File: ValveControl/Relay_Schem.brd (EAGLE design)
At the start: 101.6 x 53.6 mm, 69 parts, among them M1 IRLZ44, M2 IRLZ44, M3 IRLZ44, M4 IRLZ44, Q1 LINEAR_REGULATOR, Q2 LINEAR_REGULATOR, Q3 LINEAR_REGULATOR, Q4 LINEAR_REGULATOR, Q5 LINEAR_REGULATOR

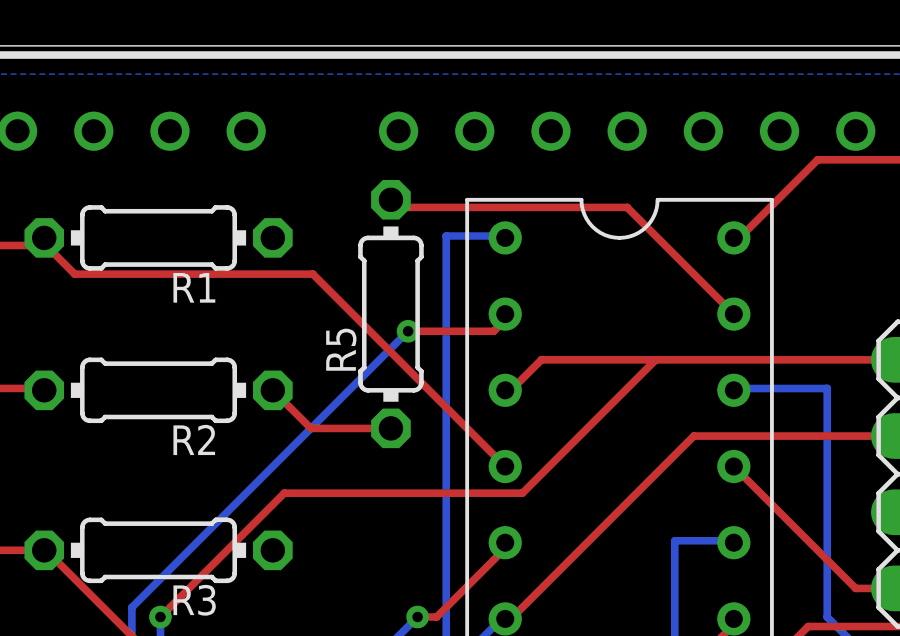
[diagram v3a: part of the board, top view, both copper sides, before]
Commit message: Some minor tweaks to the layout
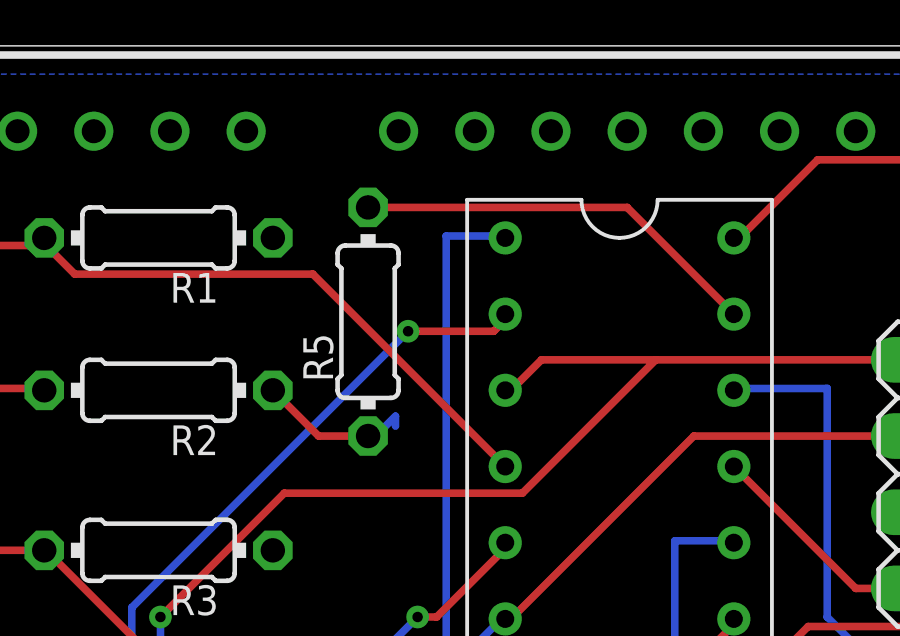
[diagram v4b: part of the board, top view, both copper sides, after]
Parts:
- moved R5 0.80 mm to (67.6, 44.5)
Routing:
- net N$10: track 13.0 -> 13.7 mm
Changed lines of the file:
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@@
 <attribute name="VALUE" x="60.1726" y="29.8704" size="0.9906" layer="27" ratio="10" rot="R180"/>
 </element>
-<element name="R5" library="rcl" library_urn="urn:adsk.eagle:library:334" package="0204/7" package3d_urn="urn:adsk.eagle:package:23498/2" value="10K" x="68.326" y="44.704" smashed="yes" rot="R90">
-<attribute name="NAME" x="67.1576" y="42.6974" size="0.9906" layer="25" ratio="10" rot="R90"/>
-<attribute name="POPULARITY" value="48" x="68.326" y="44.704" size="1.778" layer="27" rot="R90" display="off"/>
-<attribute name="SPICEPREFIX" value="R" x="68.326" y="44.704" size="1.778" layer="27" rot="R90" display="off"/>
-<attribute name="VALUE" x="66.8274" y="45.1104" size="0.9906" layer="27" ratio="10" rot="R90"/>
+<element name="R5" library="rcl" library_urn="urn:adsk.eagle:library:334" package="0204/7" package3d_urn="urn:adsk.eagle:package:23498/2" value="10K" x="67.564" y="44.45" smashed="yes" rot="R90">
+<attribute name="NAME" x="66.3956" y="42.4434" size="0.9906" layer="25" ratio="10" rot="R90"/>
+<attribute name="POPULARITY" value="48" x="67.564" y="44.45" size="1.778" layer="27" rot="R90" display="off"/>
+<attribute name="SPICEPREFIX" value="R" x="67.564" y="44.45" size="1.778" layer="27" rot="R90" display="off"/>
+<attribute name="VALUE" x="66.0654" y="44.8564" size="0.9906" layer="27" ratio="10" rot="R90"/>
 </element>
 <element name="R6" library="rcl" library_urn="urn:adsk.eagle:library:334" package="0204/7" package3d_urn="urn:adsk.eagle:package:23498/2" value="10K" x="63.246" y="21.59" smashed="yes" rot="R180">
@@
 <contactref element="M3" pad="3"/>
 <contactref element="M4" pad="3"/>
-<wire x1="68.4784" y1="41.3004" x2="68.326" y2="41.148" width="0.254" layer="16"/>
-<wire x1="68.326" y1="41.148" x2="68.326" y2="40.894" width="0.254" layer="16"/>
+<wire x1="68.4784" y1="41.3004" x2="67.818" y2="40.64" width="0.254" layer="16"/>
+<wire x1="67.818" y1="40.64" x2="67.564" y2="40.64" width="0.254" layer="16"/>
 <wire x1="68.4784" y1="40.97019375" x2="68.4784" y2="41.3004" width="0.254" layer="16"/>
-<wire x1="65.659" y1="40.894" x2="68.326" y2="40.894" width="0.254" layer="1"/>
-<wire x1="64.389" y1="42.164" x2="65.659" y2="40.894" width="0.254" layer="1"/>
+<wire x1="65.913" y1="40.64" x2="67.564" y2="40.64" width="0.254" layer="1"/>
+<wire x1="64.389" y1="42.164" x2="65.913" y2="40.64" width="0.254" layer="1"/>
 </signal>
 <signal name="N$8">
@@
 <contactref element="MUX" pad="P$15"/>
 <wire x1="76.2" y1="48.26" x2="79.756" y2="44.704" width="0.254" layer="1"/>
-<wire x1="68.58" y1="48.26" x2="76.2" y2="48.26" width="0.254" layer="1"/>
-<wire x1="68.58" y1="48.26" x2="68.326" y2="48.514" width="0.254" layer="1"/>
+<wire x1="67.564" y1="48.26" x2="76.2" y2="48.26" width="0.254" layer="1"/>
 </signal>
 <signal name="4A">

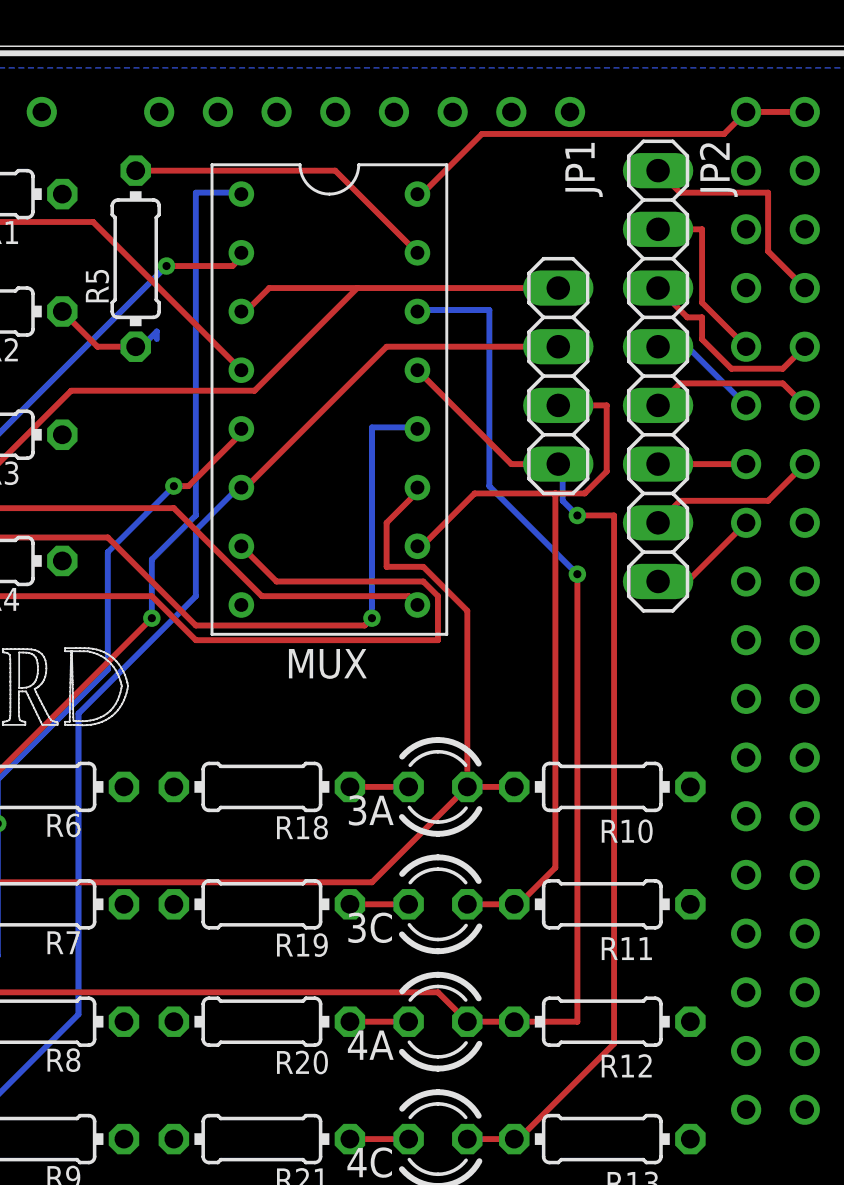
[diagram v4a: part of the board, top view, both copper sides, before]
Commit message: Add pin numbers to valve pin selection jumper header
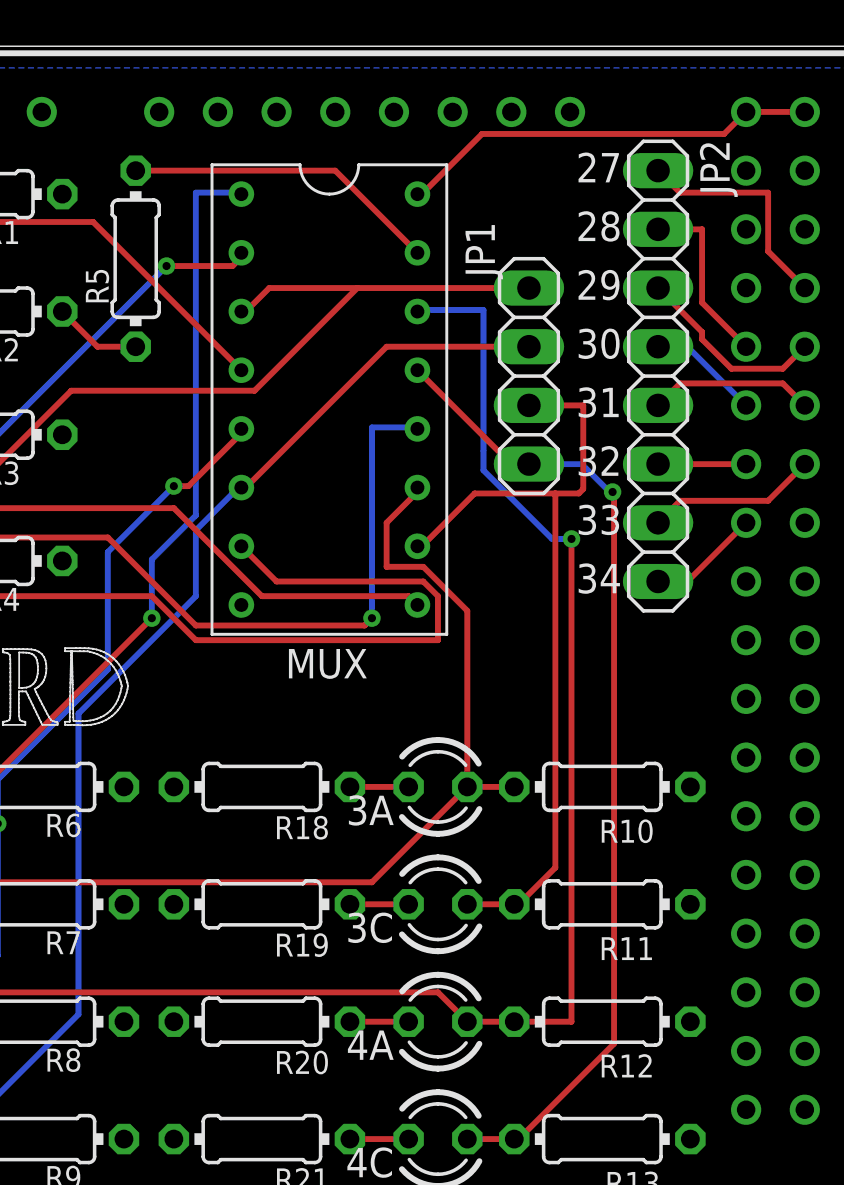
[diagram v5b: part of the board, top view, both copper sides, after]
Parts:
- moved JP1 1.27 mm to (84.6, 39.4)
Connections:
- net N$25 renamed D27
- net N$26 renamed D28
- net N$27 renamed D29
- net N$28 renamed D30
- net N$29 renamed D31
- net N$30 renamed D32
- net N$31 renamed D33
- net N$32 renamed D34
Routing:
- net 2B: track 52.2 -> 51.0 mm
- net 1B: track 55.2 -> 53.9 mm
- net 0: track 5.32 -> 4.06 mm
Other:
- board text added: "27"
- board text added: "28"
- board text added: "29"
- board text added: "30"
- board text added: "31"
- board text added: "32"
- board text added: "33"
- board text added: "34"
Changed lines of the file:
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@@
 <wire x1="50.05426875" y1="26.304990625" x2="49.91523125" y2="26.21546875" width="0.0762" layer="21"/>
 <wire x1="49.90591875" y1="26.2128" x2="49.65188125" y2="26.016409375" width="0.0762" layer="21"/>
+<text x="86.614" y="47.752" size="1.27" layer="21">27</text>
+<text x="86.614" y="45.212" size="1.27" layer="21">28</text>
+<text x="86.614" y="42.672" size="1.27" layer="21">29</text>
+<text x="86.614" y="40.132" size="1.27" layer="21">30</text>
+<text x="86.614" y="37.592" size="1.27" layer="21">31</text>
+<text x="86.614" y="35.052" size="1.27" layer="21">32</text>
+<text x="86.614" y="32.512" size="1.27" layer="21">33</text>
+<text x="86.614" y="29.972" size="1.27" layer="21">34</text>
 </plain>
 <attributes>
@@
 <attribute name="NAME" x="11.938" y="1.524" size="1.27" layer="21" rot="R90"/>
 </element>
-<element name="JP1" library="pinhead" library_urn="urn:adsk.eagle:library:325" package="1X04" package3d_urn="urn:adsk.eagle:package:22407/2" value="" x="85.852" y="39.37" smashed="yes" rot="R270">
-<attribute name="NAME" x="86.1568" y="49.6062" size="1.27" layer="25" ratio="10" rot="R270"/>
-<attribute name="POPULARITY" value="91" x="85.852" y="39.37" size="1.778" layer="27" rot="R270" display="off"/>
-<attribute name="VALUE" x="82.677" y="44.45" size="1.27" layer="27" rot="R270"/>
+<element name="JP1" library="pinhead" library_urn="urn:adsk.eagle:library:325" package="1X04" package3d_urn="urn:adsk.eagle:package:22407/2" value="" x="84.582" y="39.37" smashed="yes" rot="R270">
+<attribute name="NAME" x="81.8388" y="46.0502" size="1.27" layer="25" ratio="10" rot="R270"/>
+<attribute name="POPULARITY" value="91" x="84.582" y="39.37" size="1.778" layer="27" rot="R270" display="off"/>
+<attribute name="VALUE" x="81.407" y="44.45" size="1.27" layer="27" rot="R270"/>
 </element>
 <element name="JP2" library="pinhead" library_urn="urn:adsk.eagle:library:325" package="1X08" package3d_urn="urn:adsk.eagle:package:22409/2" value="" x="90.17" y="39.37" smashed="yes" rot="R270">
@@
 <contactref element="M3" pad="3"/>
 <contactref element="M4" pad="3"/>
-<wire x1="68.4784" y1="41.3004" x2="67.818" y2="40.64" width="0.254" layer="16"/>
 <wire x1="67.818" y1="40.64" x2="67.564" y2="40.64" width="0.254" layer="16"/>
-<wire x1="68.4784" y1="40.97019375" x2="68.4784" y2="41.3004" width="0.254" layer="16"/>
 <wire x1="65.913" y1="40.64" x2="67.564" y2="40.64" width="0.254" layer="1"/>
 <wire x1="64.389" y1="42.164" x2="65.913" y2="40.64" width="0.254" layer="1"/>
@@
 <contactref element="C8" pad="1"/>
 <contactref element="Q4" pad="3"/>
-<wire x1="82.8675" y1="42.2275" x2="80.01" y2="42.2275" width="0.254" layer="16"/>
-<wire x1="82.8675" y1="34.6075" x2="82.8675" y2="42.2275" width="0.254" layer="16"/>
-<wire x1="86.6775" y1="30.7975" x2="82.8675" y2="34.6075" width="0.254" layer="16"/>
-<wire x1="86.6775" y1="11.43" x2="86.6775" y2="30.7975" width="0.254" layer="1"/>
-<wire x1="83.947" y1="11.43" x2="86.6775" y2="11.43" width="0.254" layer="1"/>
+<wire x1="82.6135" y1="42.2275" x2="80.01" y2="42.2275" width="0.254" layer="16"/>
+<wire x1="82.6135" y1="36.1315" x2="82.6135" y2="42.2275" width="0.254" layer="16"/>
+<wire x1="86.4235" y1="11.43" x2="86.4235" y2="32.3215" width="0.254" layer="1"/>
+<wire x1="83.947" y1="11.43" x2="86.4235" y2="11.43" width="0.254" layer="1"/>
 <wire x1="80.01" y1="42.2275" x2="79.756" y2="42.164" width="0.254" layer="16"/>
 <wire x1="83.947" y1="11.43" x2="81.915" y2="11.43" width="0.254" layer="1"/>
 <wire x1="81.915" y1="11.43" x2="80.645" y2="12.7" width="0.254" layer="1"/>
-<via x="86.6775" y="30.7975" extent="1-16" drill="0.35"/>
+<via x="86.4235" y="32.3215" extent="1-16" drill="0.35"/>
 <wire x1="34.29" y1="11.43" x2="20.32" y2="11.43" width="0.254" layer="16"/>
 <wire x1="35.56" y1="10.16" x2="34.29" y2="11.43" width="0.254" layer="1"/>
@@
 <wire x1="20.32" y1="11.43" x2="19.779" y2="10.889" width="0.254" layer="16"/>
 <wire x1="19.779" y1="10.889" x2="19.779" y2="9.652" width="0.254" layer="16"/>
+<wire x1="82.6135" y1="36.1315" x2="82.6135" y2="35.29371875" width="0.254" layer="16"/>
+<wire x1="82.6135" y1="35.29371875" x2="85.58571875" y2="32.3215" width="0.254" layer="16"/>
+<wire x1="85.58571875" y1="32.3215" x2="86.4235" y2="32.3215" width="0.254" layer="16"/>
 </signal>
 <signal name="1A">
@@
 <wire x1="59.436" y1="16.51" x2="57.15" y2="16.51" width="0.254" layer="1"/>
 <wire x1="73.3425" y1="43.18" x2="72.39" y2="42.2275" width="0.254" layer="1"/>
-<wire x1="85.852" y1="43.18" x2="77.1525" y2="43.18" width="0.254" layer="1"/>
+<wire x1="84.582" y1="43.18" x2="77.1525" y2="43.18" width="0.254" layer="1"/>
 <wire x1="77.1525" y1="43.18" x2="73.3425" y2="43.18" width="0.254" layer="1"/>
 <wire x1="72.39" y1="42.2275" x2="72.136" y2="42.164" width="0.254" layer="1"/>
@@
 <wire x1="59.436" y1="6.35" x2="57.15" y2="6.35" width="0.254" layer="1"/>
 <wire x1="78.4225" y1="40.64" x2="72.39" y2="34.6075" width="0.254" layer="1"/>
-<wire x1="85.852" y1="40.64" x2="78.4225" y2="40.64" width="0.254" layer="1"/>
+<wire x1="84.582" y1="40.64" x2="78.4225" y2="40.64" width="0.254" layer="1"/>
 <wire x1="72.39" y1="34.6075" x2="72.136" y2="34.544" width="0.254" layer="1"/>
 <wire x1="65.0875" y1="11.7475" x2="59.69" y2="6.35" width="0.254" layer="16"/>
@@
 <wire x1="83.947" y1="6.35" x2="81.915" y2="6.35" width="0.254" layer="1"/>
 <wire x1="83.82" y1="35.56" x2="79.756" y2="39.624" width="0.254" layer="1"/>
-<wire x1="85.852" y1="35.56" x2="83.82" y2="35.56" width="0.254" layer="1"/>
+<wire x1="84.582" y1="35.56" x2="83.82" y2="35.56" width="0.254" layer="1"/>
 <wire x1="88.265" y1="10.4775" x2="84.1375" y2="6.35" width="0.254" layer="1"/>
-<wire x1="88.265" y1="33.3375" x2="88.265" y2="10.4775" width="0.254" layer="1"/>
-<wire x1="86.6775" y1="33.3375" x2="88.265" y2="33.3375" width="0.254" layer="1"/>
-<wire x1="86.0425" y1="33.9725" x2="86.6775" y2="33.3375" width="0.254" layer="16"/>
-<wire x1="86.0425" y1="35.56" x2="86.0425" y2="33.9725" width="0.254" layer="16"/>
+<wire x1="88.265" y1="34.3535" x2="88.265" y2="10.4775" width="0.254" layer="1"/>
+<wire x1="88.265" y1="34.3535" x2="88.2015" y2="34.3535" width="0.254" layer="1"/>
 <wire x1="84.1375" y1="6.35" x2="83.947" y2="6.35" width="0.254" layer="1"/>
-<wire x1="86.0425" y1="35.56" x2="85.852" y2="35.56" width="0.254" layer="16"/>
-<via x="86.6775" y="33.3375" extent="1-16" drill="0.35"/>
+<via x="88.2015" y="34.3535" extent="1-16" drill="0.35"/>
+<wire x1="88.2015" y1="34.3535" x2="88.0745" y2="34.3535" width="0.254" layer="16"/>
+<wire x1="88.0745" y1="34.3535" x2="86.868" y2="35.56" width="0.254" layer="16"/>
+<wire x1="84.582" y1="35.56" x2="86.868" y2="35.56" width="0.254" layer="16"/>
 </signal>
 <signal name="4Y">
@@
 <wire x1="83.947" y1="16.51" x2="81.915" y2="16.51" width="0.254" layer="1"/>
 <wire x1="82.2325" y1="34.29" x2="80.01" y2="32.0675" width="0.254" layer="1"/>
-<wire x1="86.995" y1="34.29" x2="85.725" y2="34.29" width="0.254" layer="1"/>
+<wire x1="86.741" y1="34.29" x2="85.725" y2="34.29" width="0.254" layer="1"/>
 <wire x1="85.725" y1="34.29" x2="82.2325" y2="34.29" width="0.254" layer="1"/>
-<wire x1="87.9475" y1="35.2425" x2="86.995" y2="34.29" width="0.254" layer="1"/>
-<wire x1="87.9475" y1="38.1" x2="87.9475" y2="35.2425" width="0.254" layer="1"/>
-<wire x1="85.852" y1="38.1" x2="87.9475" y2="38.1" width="0.254" layer="1"/>
+<wire x1="86.9315" y1="34.4805" x2="86.741" y2="34.29" width="0.254" layer="1"/>
+<wire x1="86.9315" y1="38.1" x2="86.9315" y2="34.4805" width="0.254" layer="1"/>
+<wire x1="84.582" y1="38.1" x2="86.9315" y2="38.1" width="0.254" layer="1"/>
 <wire x1="80.01" y1="32.0675" x2="79.756" y2="32.004" width="0.254" layer="1"/>
 <wire x1="85.725" y1="18.0975" x2="84.1375" y2="16.51" width="0.254" layer="1"/>
@@
 <wire x1="51.435" y1="46.99" x2="51.689" y2="46.99" width="0.254" layer="1"/>
 </signal>
-<signal name="N$25">
+<signal name="D27">
 <contactref element="U$2" pad="27"/>
 <contactref element="JP2" pad="1"/>
@@
 <wire x1="90.17" y1="48.26" x2="91.1225" y2="47.3075" width="0.254" layer="1"/>
 </signal>
-<signal name="N$26">
+<signal name="D28">
 <contactref element="U$2" pad="28"/>
 <contactref element="JP2" pad="2"/>
@@
 <wire x1="90.17" y1="45.72" x2="92.075" y2="45.72" width="0.254" layer="1"/>
 </signal>
-<signal name="N$27">
+<signal name="D29">
 <contactref element="U$2" pad="29"/>
 <contactref element="JP2" pad="3"/>
@@
 <wire x1="93.345" y1="39.6875" x2="95.5675" y2="39.6875" width="0.254" layer="1"/>
 <wire x1="92.075" y1="40.9575" x2="93.345" y2="39.6875" width="0.254" layer="1"/>
-<wire x1="92.075" y1="41.91" x2="92.075" y2="40.9575" width="0.254" layer="1"/>
-<wire x1="91.44" y1="41.91" x2="92.075" y2="41.91" width="0.254" layer="1"/>
-<wire x1="90.17" y1="43.18" x2="91.44" y2="41.91" width="0.254" layer="1"/>
-</signal>
-<signal name="N$28">
+<wire x1="92.075" y1="41.275" x2="92.075" y2="40.9575" width="0.254" layer="1"/>
+<wire x1="90.17" y1="43.18" x2="92.075" y2="41.275" width="0.254" layer="1"/>
+</signal>
+<signal name="D30">
 <contactref element="U$2" pad="30"/>
 <contactref element="JP2" pad="4"/>
@@
 <wire x1="90.17" y1="40.64" x2="91.44" y2="40.64" width="0.254" layer="16"/>
 </signal>
-<signal name="N$29">
+<signal name="D31">
 <contactref element="U$2" pad="31"/>
 <contactref element="JP2" pad="5"/>
@@
 <wire x1="90.17" y1="38.1" x2="91.1225" y2="39.0525" width="0.254" layer="1"/>
 </signal>
-<signal name="N$30">
+<signal name="D32">
 <contactref element="U$2" pad="32"/>
 <contactref element="JP2" pad="6"/>
 <wire x1="90.17" y1="35.56" x2="93.98" y2="35.56" width="0.254" layer="1"/>
 </signal>
-<signal name="N$31">
+<signal name="D33">
 <contactref element="U$2" pad="33"/>
 <contactref element="JP2" pad="7"/>
@@
 <wire x1="90.17" y1="33.02" x2="91.1225" y2="33.9725" width="0.254" layer="1"/>
 </signal>
-<signal name="N$32">
+<signal name="D34">
 <contactref element="U$2" pad="34"/>
 <contactref element="JP2" pad="8"/>
